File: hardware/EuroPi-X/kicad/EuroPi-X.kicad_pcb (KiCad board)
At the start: 2 copper layers, 102.9 x 109.2 mm, 164 parts, among them J1 Conn_01x16_Pin, J10 Thonkiconn_Mono_Jack, J11 Conn_02x08_Odd_Even, J12 Thonkiconn_Mono_Jack, J13 Thonkiconn_Mono_Jack, J14 Thonkiconn_Mono_Jack, J15 Thonkiconn_Mono_Jack, J16 Thonkiconn_Mono_Jack, J17 Thonkiconn_Mono_Jack, J18 Conn_01x03_Pin, J2 Conn_01x16_Pin, J22 Conn_01x11_Pin, J3 Thonkiconn_Mono_Jack, J4 Thonkiconn_Mono_Jack, J5 Conn_01x16_Pin, J6 Thonkiconn_Mono_Jack, J7 Thonkiconn_Mono_Jack, J8 Conn_01x16_Pin, J9 Thonkiconn_Mono_Jack, P1 USB_C_Plug_USB2.0, P2 Potentiometer_9mm_Vertical_Li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, P3 Potentiometer_9mm_Vertical_Li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, Q1 BSS138, SW1 B1, SW2 B2, U1 MCP6002-xSN, U10 MCP3428, U11 L7805, U12 LM4040DBZ-4.1, U2 LM4040DBZ-2.0, U3 LM4040DBZ-10, U4 RP2040, U7 TL074, U8 TL074, U9 MCP6004, Y1 Crystal_GND2

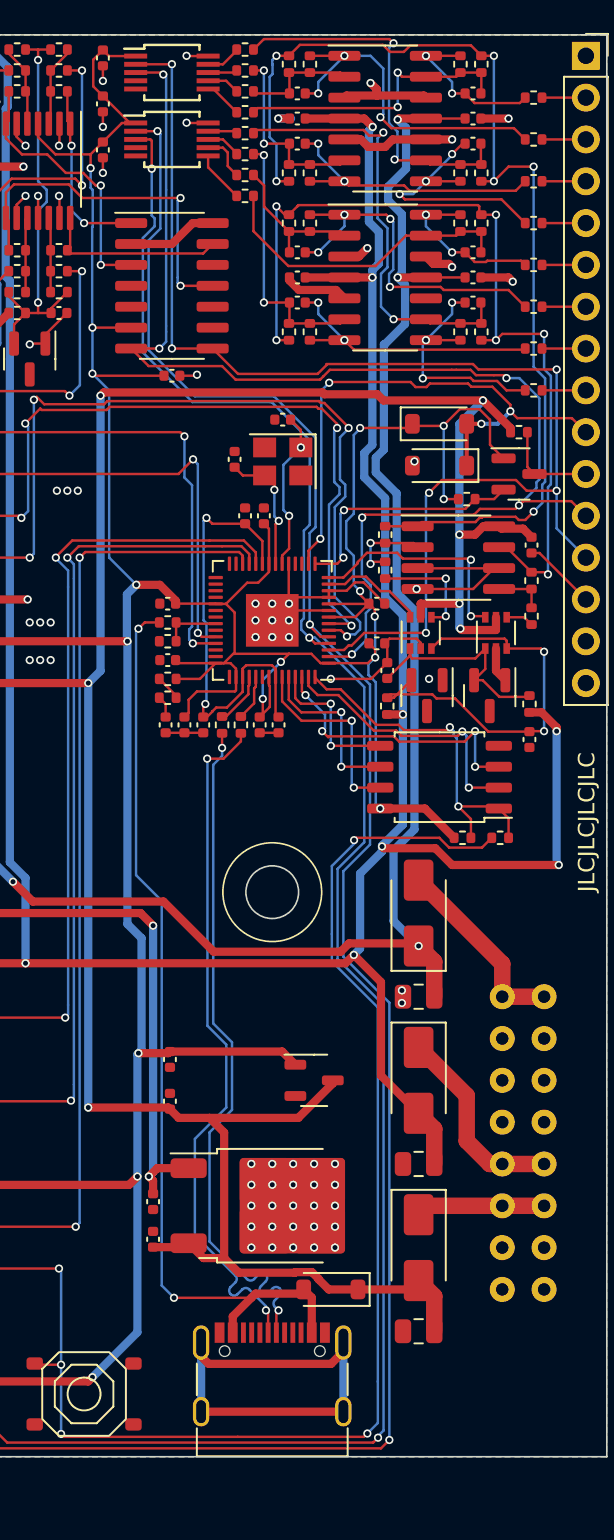
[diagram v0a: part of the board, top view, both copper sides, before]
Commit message: add qr
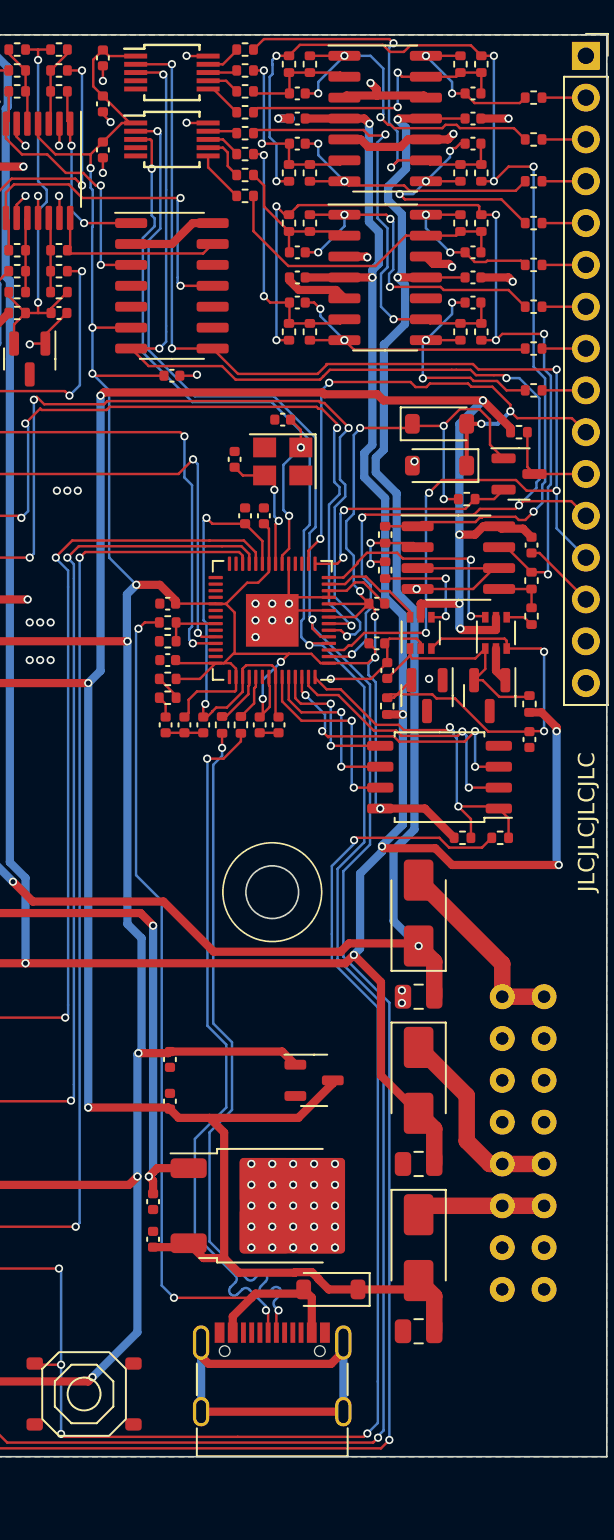
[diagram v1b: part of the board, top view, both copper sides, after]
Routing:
- net Net-(U7C--): track 23.0 -> 23.9 mm
- net Earth: vias 70 -> 68

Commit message: save
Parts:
- added G***: LOGO, LOGO, B.Cu at (82.5, 31.8)
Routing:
- net /ADC_INPUT_2: track 16.5 -> 17.4 mm
- net /NEOPIXEL_DATA_3V3: track 15.1 -> 15.9 mm
- net /KNOB_1: track 26.5 -> 25.8 mm
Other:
- board text added: "version 1.1"
